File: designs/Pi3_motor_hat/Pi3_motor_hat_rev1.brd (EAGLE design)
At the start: 65 x 56.1 mm, 16 parts, among them X1 RASPI_BOARD_B+#_HDC, X2 22-23-2021

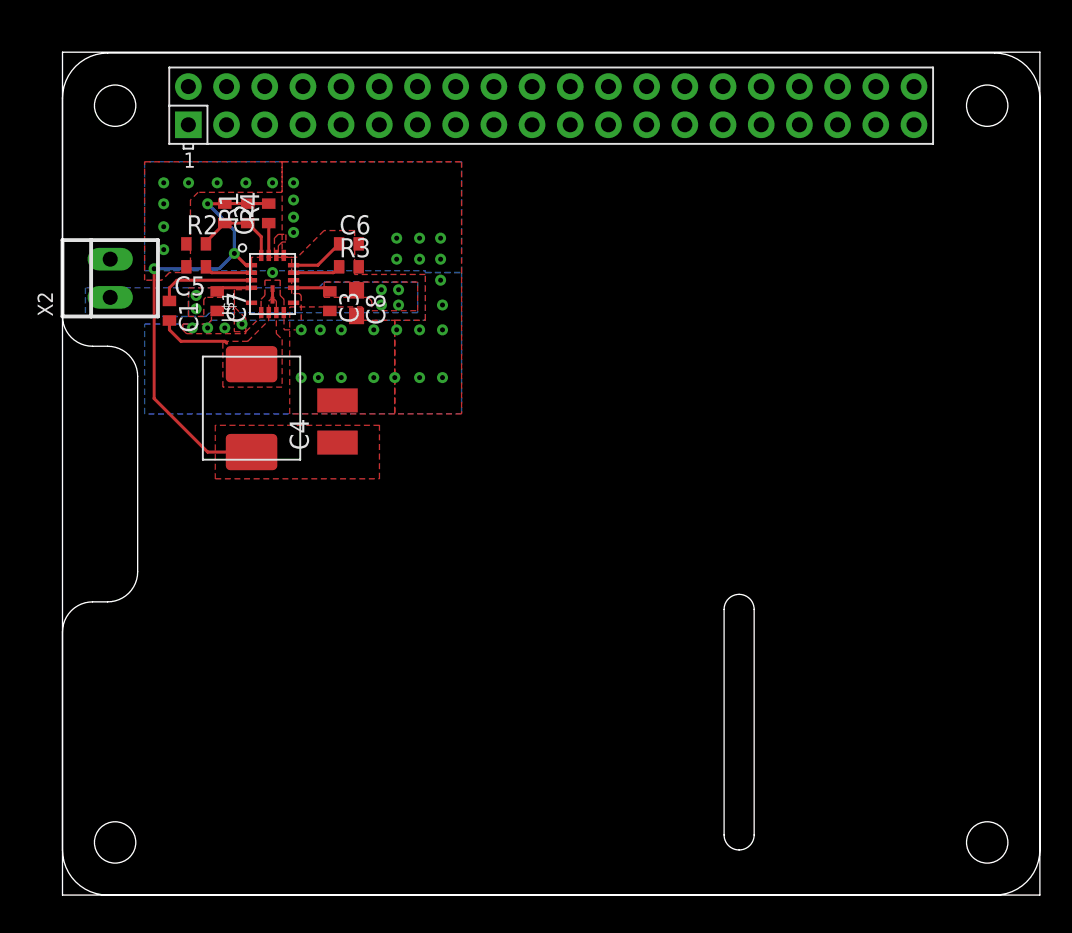
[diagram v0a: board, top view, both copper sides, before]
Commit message: Add part for Pi3 hats
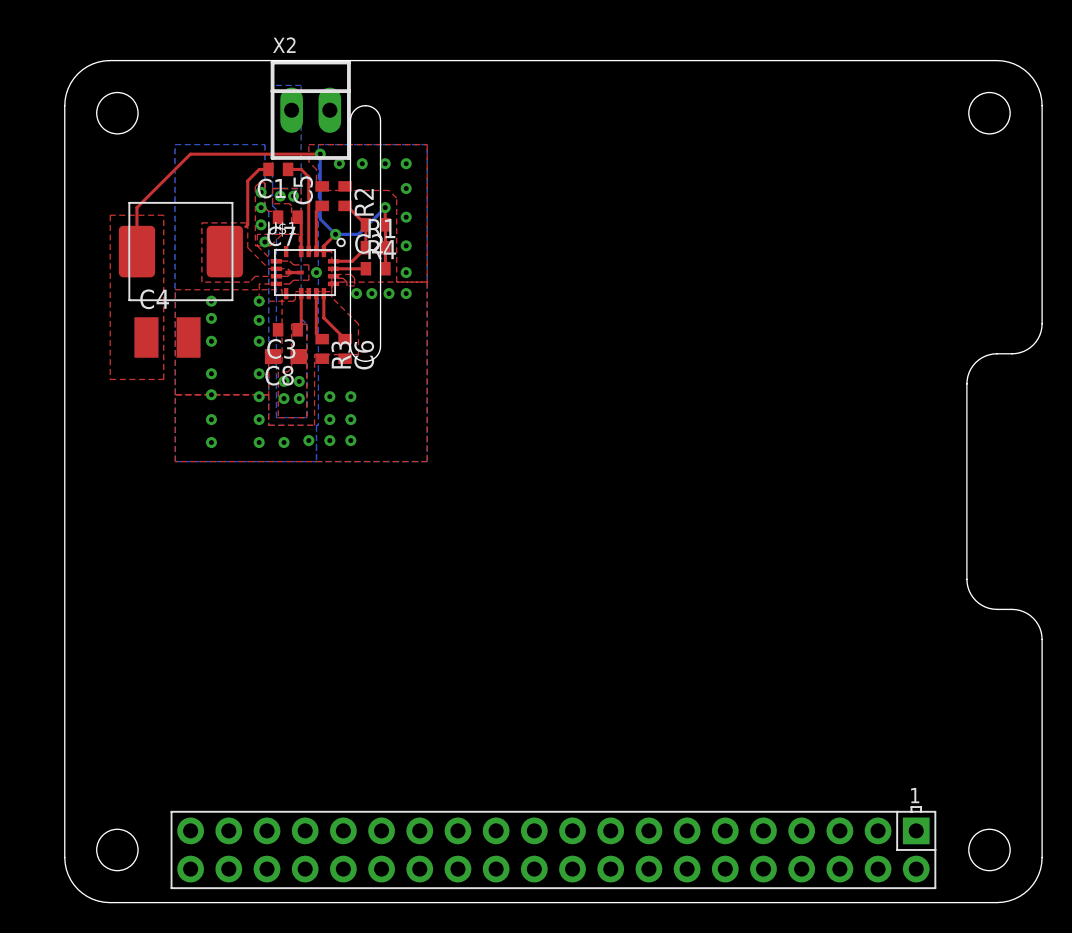
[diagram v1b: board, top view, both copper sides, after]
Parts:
- moved X1 85.6 mm to (65.2, 55.5), turned to 180 degrees
- moved X2 17.4 mm to (16.5, 52.2), turned to 0 degrees
- moved C4 12.6 mm to (6.99, 37.1), turned to 0 degrees
- moved C1 11.9 mm to (14.4, 48.3), turned to 180 degrees
- moved L1 11.4 mm to (7.87, 42.8), turned to 180 degrees
- moved R2 10.4 mm to (18.8, 46.5), turned to 270 degrees
- moved C2 10.1 mm to (20.8, 44.6), turned to 180 degrees
- moved C5 9.61 mm to (17.3, 46.5), turned to 90 degrees
- moved R1 8.81 mm to (20.8, 43.1), turned to 0 degrees
- moved R4 8.01 mm to (20.8, 41.7), turned to 0 degrees
- moved C7 7.30 mm to (15.0, 45.1), turned to 180 degrees
- moved C6 6.99 mm to (18.8, 36.3), turned to 270 degrees
- moved C8 5.89 mm to (14.9, 35.8), turned to 180 degrees
- moved R3 5.74 mm to (17.3, 36.3), turned to 270 degrees
- moved C3 3.38 mm to (15.0, 37.6), turned to 180 degrees
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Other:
- board size 65 x 56.1 mm -> 65 x 56 mm
